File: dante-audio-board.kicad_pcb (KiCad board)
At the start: 2 copper layers, 25.5 x 57.8 mm, 1 part

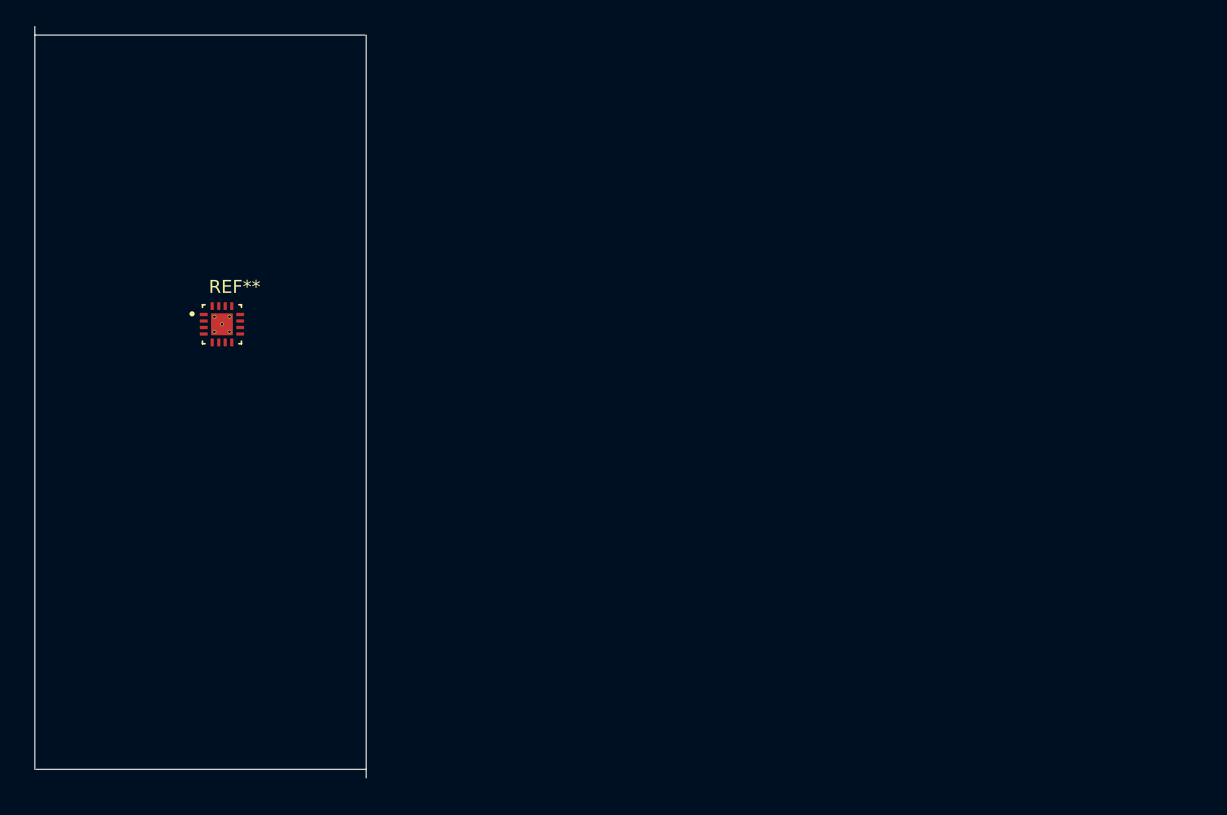
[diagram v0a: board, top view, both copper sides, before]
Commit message: stab at HAT dimensions
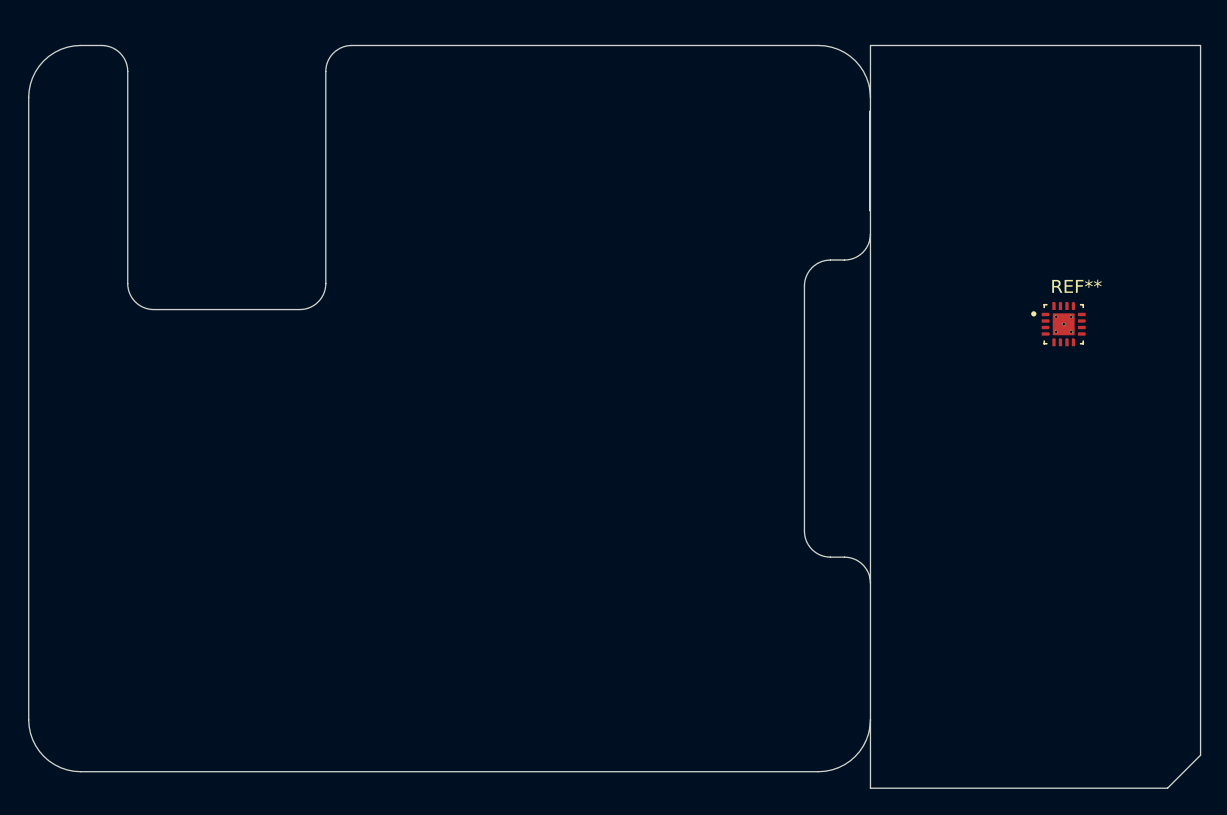
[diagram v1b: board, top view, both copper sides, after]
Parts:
- moved REF** 64.8 mm to (129.2, 72.2)
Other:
- board size 25.5 x 57.8 mm -> 90.2 x 57.2 mm

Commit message: fix basic 4 layer stackup
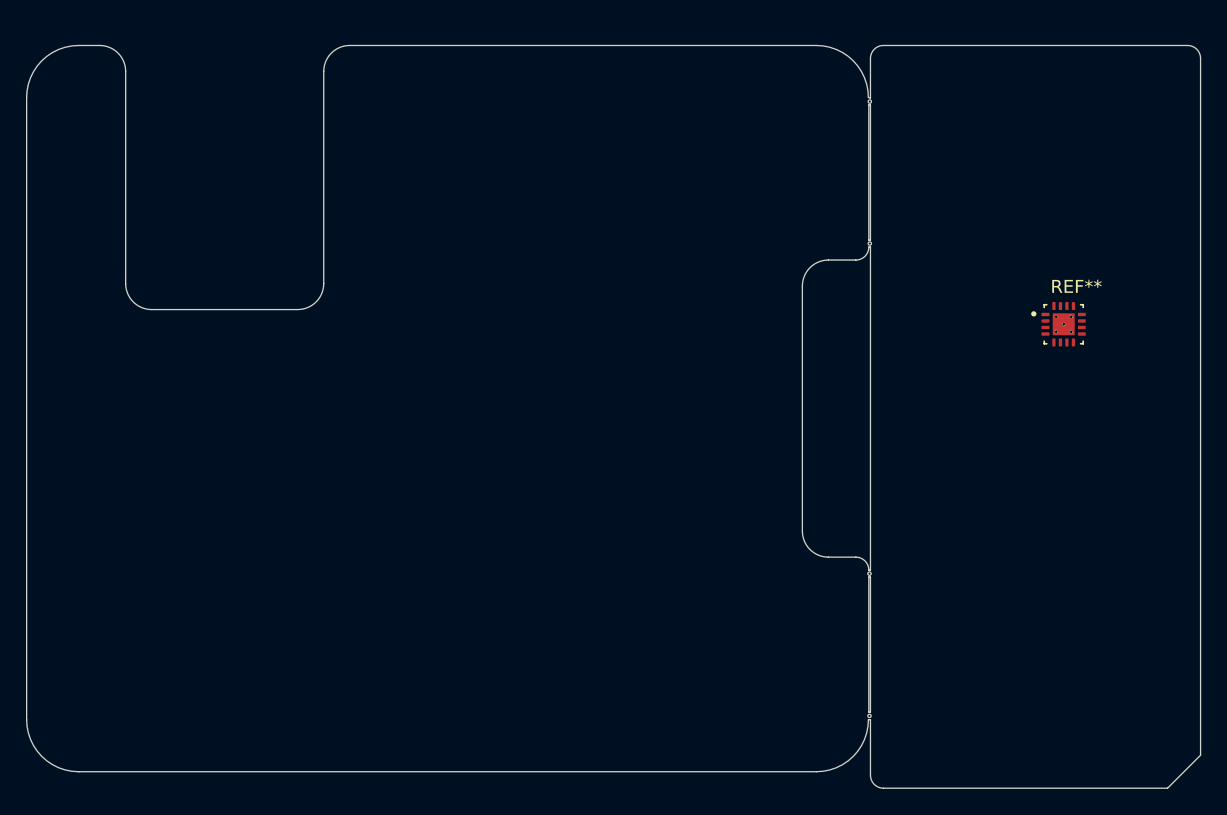
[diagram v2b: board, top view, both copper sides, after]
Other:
- board size 90.2 x 57.2 mm -> 90.3 x 57.2 mm
- copper layers 2 -> 4
- rule pad_to_mask_clearance: 0 -> 2
- board text added: "0"
- board text added: "0 mm"
- board text added: "0.01 mm"
- board text added: "0.02"
- board text added: "0.035 mm"
- board text added: "0.1 mm"
- board text added: "0.1270 mm / 0.1270 mm"
- board text added: "0.2032 mm"
- board text added: "1"
- board text added: "1.24 mm"
- board text added: "1.6000 mm"
- board text added: "3.3"
- board text added: "4"
- board text added: "4.5"
- board text added: "90.3290 mm x 57.1500 mm"
- board text added: "B.Cu"
- board text added: "B.Mask"
- board text added: "B.Paste"
- board text added: "B.Silkscreen"
- board text added: "BOARD CHARACTERISTICS"
- board text added: "Board Thickness:"
- board text added: "Board overall dimensions:"
- board text added: "Bottom Silk Screen"
- board text added: "Bottom Solder Mask"
- board text added: "Bottom Solder Paste"
- board text added: "Castellated pads:"
- board text added: "Color"
- board text added: "Copper Finish:"
- board text added: "Copper Layer Count:"
- board text added: "Dielectric 1"
- board text added: "Dielectric 2"
- board text added: "Dielectric 3"
- board text added: "Edge card connectors:"
- board text added: "Epsilon R"
- board text added: "F.Cu"
- board text added: "F.Mask"
- board text added: "F.Paste"
- board text added: "F.Silkscreen"
- board text added: "FR4"
- board text added: "Impedance Control:"
- board text added: "In1.Cu"
- board text added: "In2.Cu"
- board text added: "Layer Name"
- board text added: "Loss Tangent"
- board text added: "Material"
- board text added: "Min hole diameter:"
- board text added: "Min track/spacing:"
- board text added: "No"
- board text added: "None"
- board text added: "Not specified"
- board text added: "Plated Board Edge:"
- board text added: "Thickness (mm)"
- board text added: "Top Silk Screen"
- board text added: "Top Solder Mask"
- board text added: "Top Solder Paste"
- board text added: "Type"
- board text added: "copper"
- board text added: "core"
- board text added: "prepreg"
